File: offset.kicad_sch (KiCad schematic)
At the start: 25 parts, among them U11 OPA2189DGK, U12 TMUX1108PW

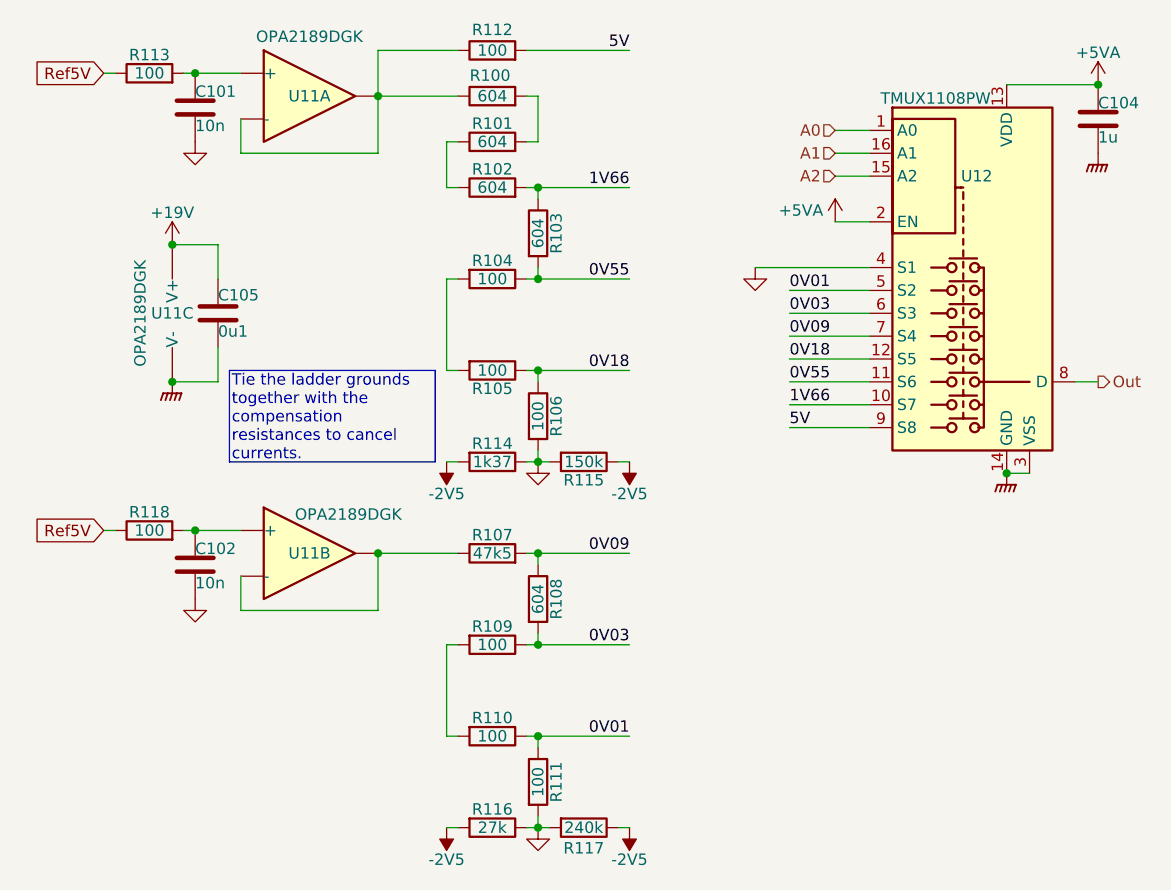
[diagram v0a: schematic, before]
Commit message: DRC update.  Repin ADC.  De-crack the S/H ground.
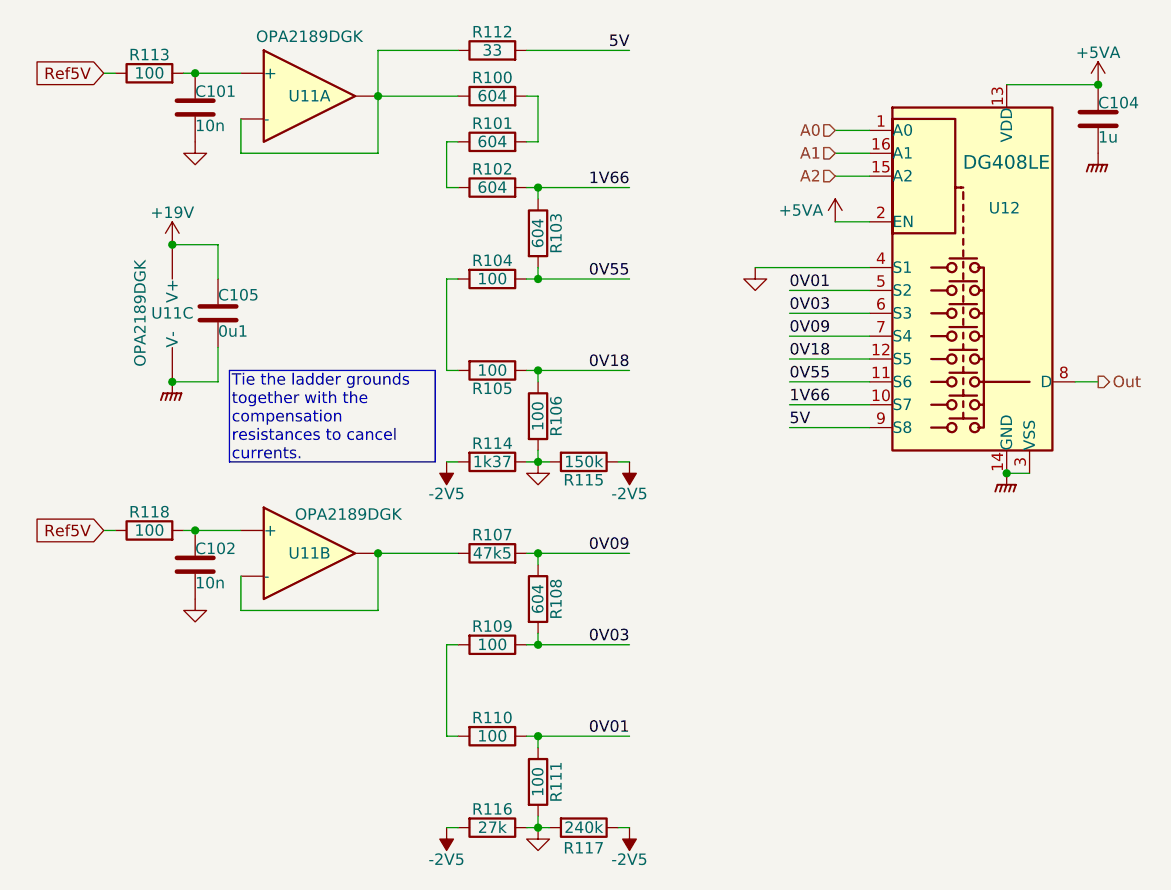
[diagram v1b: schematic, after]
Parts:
- R112: value 100 -> 33; LCSC C25076 -> C25105
- U12: value TMUX1108PW -> DG408LE; symbol Analog_Switch:TMUX1108PW -> Parts:DG408LE; now in the parts list
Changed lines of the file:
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@@
 	)
 	(symbol
-		(lib_id "Analog_Switch:TMUX1108PW")
+		(lib_id "Parts:DG408LE")
 		(at 180.34 81.28 0)
 		(unit 1)
 		(exclude_from_sim no)
-		(in_bom no)
+		(in_bom yes)
 		(on_board yes)
 		(dnp no)
 		(property "Reference" "U12"
-			(at 180.34 68.58 0)
-			(effects
-				(font
-					(size 1.27 1.27)
-				)
-				(justify left)
-			)
-		)
-		(property "Value" "TMUX1108PW"
-			(at 183.642 59.944 0)
-			(effects
-				(font
-					(size 1.27 1.27)
+			(at 185.166 72.136 0)
+			(effects
+				(font
+					(size 1.27 1.27)
+				)
+			)
+		)
+		(property "Value" "DG408LE"
+			(at 190.246 67.056 0)
+			(effects
+				(font
+					(size 1.524 1.524)
 				)
 				(justify right)
@@
 			)
 		)
-		(property "Description" "5V / ±2.5V, Low-Leakage-Current, 8:1 Precision Multiplexer, 2.5 Ohm Ron, 90Mhz, TSSOP-16"
+		(property "Description" "Low-Leakage-Current, 8:1 Precision Multiplexer, TSSOP-16"
 			(at 180.34 81.28 0)
 			(effects
@@
 		(dnp no)
 		(property "Reference" "R112"
-			(at 128.27 52.324 90)
-			(effects
-				(font
-					(size 1.27 1.27)
-				)
-			)
-		)
-		(property "Value" "100"
+			(at 128.27 52.578 90)
+			(effects
+				(font
+					(size 1.27 1.27)
+				)
+			)
+		)
+		(property "Value" "33"
 			(at 128.27 54.61 90)
 			(effects
@@
 			)
 		)
-		(property "LCSC" "C25076"
+		(property "LCSC" "C25105"
 			(at 128.27 54.61 90)
 			(effects
@@
 		(dnp no)
 		(property "Reference" "R100"
-			(at 128.016 57.404 90)
-			(effects
-				(font
+			(at 128.27 57.658 90)
+			(effects
+				(font

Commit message: More component metadata.
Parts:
- C101, C102, C104, C105, R112, R113, R115, R118: Stock (none) -> JLC
- R100, R101, R102, R103, R104, R105, R106, R107, R108, R109, R110, R111: Stock (none) -> Digikey
- R116: LCSC (none) -> C22967; Stock (none) -> JLC
- R117: LCSC (none) -> C4197; Stock (none) -> JLC
- U12: Stock 3 -> ?
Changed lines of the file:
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@@
 			)
 		)
-		(property "Stock" ""
+		(property "Stock" "Digikey"
 			(at 128.27 64.77 90)
 			(effects
@@
 			)
 		)
-		(property "Stock" ""
+		(property "Stock" "JLC"
 			(at 128.27 140.97 90)
 			(effects
@@
 			)
 		)
-		(property "LCSC" ""
+		(property "LCSC" "C22967"
 			(at 128.27 140.97 90)
 			(effects
@@
 			)
 		)
-		(property "Stock" ""
+		(property "Stock" "Digikey"
 			(at 128.27 110.49 90)
 			(effects
@@
 			)
 		)
-		(property "Stock" ""
+		(property "Stock" "JLC"
 			(at 95.25 60.96 0)
 			(effects
@@
 			)
 		)
-		(property "Stock" "3"
+		(property "Stock" "?"
 			(at 180.34 81.28 0)
 			(effects
@@
 			)
 		)
-		(property "Stock" ""
+		(property "Stock" "Digikey"
 			(at 128.27 80.01 90)
 			(effects
@@
 			)
 		)
-		(property "Stock" ""
+		(property "Stock" "JLC"
 			(at 128.27 54.61 90)
 			(effects
@@
 			)
 		)
-		(property "Stock" ""
+		(property "Stock" "Digikey"
 			(at 128.27 90.17 90)
 			(effects
@@
 			)
 		)
-		(property "Stock" ""
+		(property "Stock" "JLC"
 			(at 97.79 83.82 0)
 			(effects
@@
 			)
 		)
-		(property "Stock" ""
+		(property "Stock" "Digikey"
 			(at 133.35 115.57 90)
 			(effects
@@
 			)
 		)
-		(property "Stock" ""
+		(property "Stock" "JLC"
 			(at 195.58 62.23 0)
 			(effects
@@
 			)
 		)
-		(property "Stock" ""
+		(property "Stock" "JLC"
 			(at 95.25 111.76 0)
 			(effects
@@
 			)
 		)
-		(property "Stock" ""
+		(property "Stock" "Digikey"
 			(at 128.27 130.81 90)
 			(effects
@@
 			)
 		)
-		(property "Stock" ""
+		(property "Stock" "Digikey"
 			(at 128.27 120.65 90)
 			(effects
@@
 			)
 		)
-		(property "Stock" ""
+		(property "Stock" "Digikey"
 			(at 133.35 95.25 90)
 			(effects
@@
 			)
 		)
-		(property "Stock" ""
+		(property "Stock" "JLC"
 			(at 138.43 100.33 90)
 			(effects
@@
 			)
 		)
-		(property "LCSC" ""
+		(property "LCSC" "C4197"
 			(at 138.43 140.97 90)
 			(effects
@@
 			)
 		)
-		(property "Stock" ""
+		(property "Stock" "JLC"
 			(at 138.43 140.97 90)
 			(effects
@@
 			)
 		)
-		(property "Stock" ""
+		(property "Stock" "Digikey"
 			(at 133.35 74.93 90)
 			(effects
@@
 			)
 		)
-		(property "Stock" ""
+		(property "Stock" "JLC"
 			(at 90.17 107.95 90)
 			(effects
@@
 			)
 		)
-		(property "Stock" ""
+		(property "Stock" "Digikey"
 			(at 128.27 59.69 90)
 			(effects
@@
 			)
 		)
-		(property "Stock" ""
+		(property "Stock" "JLC"
 			(at 90.17 57.15 90)
 			(effects
@@
 			)
 		)
-		(property "Stock" ""
+		(property "Stock" "Digikey"
 			(at 128.27 69.85 90)
 			(effects
@@
 			)
 		)
-		(property "Stock" ""
+		(property "Stock" "Digikey"
 			(at 133.35 135.89 90)
 			(effects

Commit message: Front panel
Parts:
- U12: LCSC C1021800 -> (none); Stock ? -> Digikey; now left out of the parts list
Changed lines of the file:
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@@
 		(unit 1)
 		(exclude_from_sim no)
-		(in_bom yes)
+		(in_bom no)
 		(on_board yes)
 		(dnp no)
@@
 			)
 		)
-		(property "LCSC" "C1021800"
+		(property "LCSC" ""
 			(at 180.34 81.28 0)
 			(effects
@@
 			)
 		)
-		(property "Stock" "?"
+		(property "Stock" "Digikey"
 			(at 180.34 81.28 0)
 			(effects

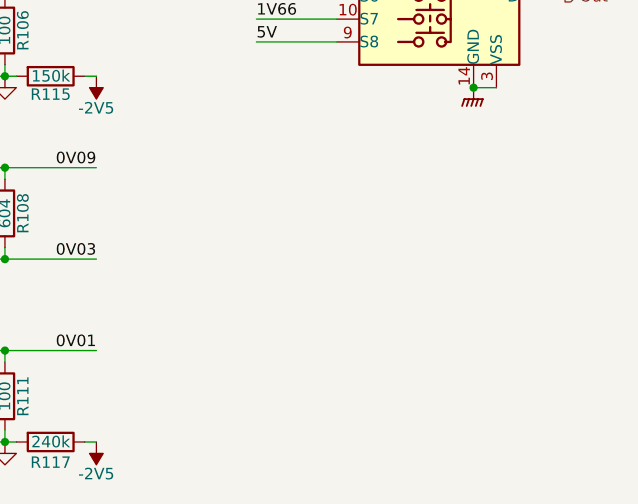
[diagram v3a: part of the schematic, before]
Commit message: Change some footprints.
Mounting holes for covers.
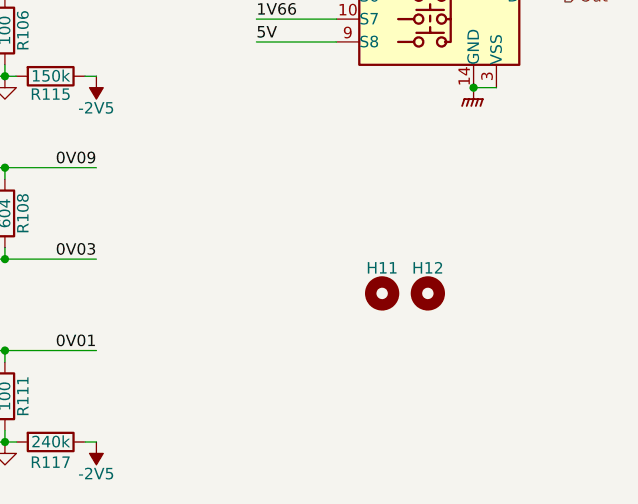
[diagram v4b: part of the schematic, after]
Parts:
- added H11, H12: MountingHole, Parts:Hole_1.5mm_Unplated, symbol Mechanical:MountingHole
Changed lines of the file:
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@@
+	)
+	(symbol
+		(lib_id "Mechanical:MountingHole")
+		(at 175.26 124.46 0)
+		(unit 1)
+		(exclude_from_sim no)
+		(in_bom no)
+		(on_board yes)
+		(dnp no)
+		(property "Reference" "H11"
+			(at 175.26 121.666 0)
+			(effects
+				(font
+					(size 1.27 1.27)
+				)
+			)
+		)
+		(property "Value" "MountingHole"
+			(at 175.26 121.285 0)
+			(effects
+				(font
+					(size 1.27 1.27)
+				)
+				(hide yes)
+			)
+		)
+		(property "Footprint" "Parts:Hole_1.5mm_Unplated"
+			(at 175.26 124.46 0)
+			(effects
+				(font
+					(size 1.27 1.27)
+				)
+				(hide yes)
+			)
+		)
+		(property "Datasheet" "~"
+			(at 175.26 124.46 0)
+			(effects
+				(font
+					(size 1.27 1.27)
+				)
+				(hide yes)
+			)
+		)
+		(property "Description" "Mounting Hole without connection"
+			(at 175.26 124.46 0)
+			(effects
+				(font
+					(size 1.27 1.27)
+				)
+				(hide yes)
+			)
+		)
+		(instances
+			(project "lincal"
+				(path "/b054cef4-39e3-49d8-aff0-7ba5a206c187/fd210975-34eb-456f-9075-cf344b0a559b"
+					(reference "H11")
+					(unit 1)
+				)
+			)
+		)
 	)
 	(symbol
@@
 					(unit 1)
 				)
+			)
+		)
+	)
+	(symbol
+		(lib_id "Mechanical:MountingHole")
+		(at 180.34 124.46 0)
+		(unit 1)
+		(exclude_from_sim no)
+		(in_bom no)
+		(on_board yes)
+		(dnp no)
+		(property "Reference" "H12"
+			(at 180.34 121.666 0)
+			(effects
+				(font
+					(size 1.27 1.27)
+				)
+			)
+		)
+		(property "Value" "MountingHole"
+			(at 180.34 121.285 0)
+			(effects
+				(font
+					(size 1.27 1.27)
+				)
+				(hide yes)
+			)
+		)
+		(property "Footprint" "Parts:Hole_1.5mm_Unplated"
+			(at 180.34 124.46 0)
+			(effects
+				(font
+					(size 1.27 1.27)
+				)
+				(hide yes)
+			)
+		)
+		(property "Datasheet" "~"
+			(at 180.34 124.46 0)
+			(effects
+				(font
+					(size 1.27 1.27)
+				)
+				(hide yes)
+			)
+		)
+		(property "Description" "Mounting Hole without connection"
+			(at 180.34 124.46 0)
+			(effects
+				(font
+					(size 1.27 1.27)
+				)
+				(hide yes)
+			)
+		)
+		(instances
+			(project "lincal"
+				(path "/b054cef4-39e3-49d8-aff0-7ba5a206c187/fd210975-34eb-456f-9075-cf344b0a559b"
+					(reference "H12")
+					(unit 1)
+				)

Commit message: Tweak various feedback loops.
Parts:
- H11, H12: Stock (none) -> Board
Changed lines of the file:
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@@
+			)
+		)
+		(property "Stock" "Board"
+			(at 175.26 124.46 0)
+			(effects
+				(font
+					(size 1.27 1.27)
+				)
+				(hide yes)
 			)
 		)
@@
 			(at 180.34 124.46 0)
 			(effects
+				(font
+					(size 1.27 1.27)
+				)
+				(hide yes)
+			)
+		)
+		(property "Stock" "Board"
+			(at 180.34 124.46 0)
+			(effects

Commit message: Readyish
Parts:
- C101, C102: LCSC C307500 -> C389113
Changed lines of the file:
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@@
 			)
 		)
-		(property "Datasheet" "C0G, 25V"
+		(property "Datasheet" "C0G, 50V"
 			(at 95.25 60.96 0)
 			(effects
@@
 			)
 		)
-		(property "LCSC" "C307500"
+		(property "LCSC" "C389113"
 			(at 95.25 60.96 0)
 			(effects
@@
 			)
 		)
-		(property "Datasheet" "C0G, 25V"
+		(property "Datasheet" "C0G, 50V"
 			(at 95.25 111.76 0)
 			(effects
@@
 			)
 		)
-		(property "LCSC" "C307500"
+		(property "LCSC" "C389113"
 			(at 95.25 111.76 0)
 			(effects
